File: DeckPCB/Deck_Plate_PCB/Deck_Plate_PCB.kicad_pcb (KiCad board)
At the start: 2 copper layers, 124.1 x 104 mm, 52 parts, among them J1 Raspberry_Pi_2_3, J2 NASA_Telemetry_Interface, J3 NASA PWR_Interface, J8 Board_to_Board, J9 Power, P1 Digital, P10 CONN_01X01, P11 CONN_01X01, P12 CONN_01X01, P13 CONN_01X01, P2 Power, P3 Analog, P4 Analog, P5 PWM, P6 PWM, P7 Communication, P8 CONN_01X01, P9 CONN_01X01, Q2 2N7000, Q3 2N7000, U2 LM2576T-5, U3 D24V25F9, U5 LM2576T-5, U6 SF_Logic_Level_Conv, U7 Lidar_RangeFinder, U8 ADXL377, U9 TTL_Camera

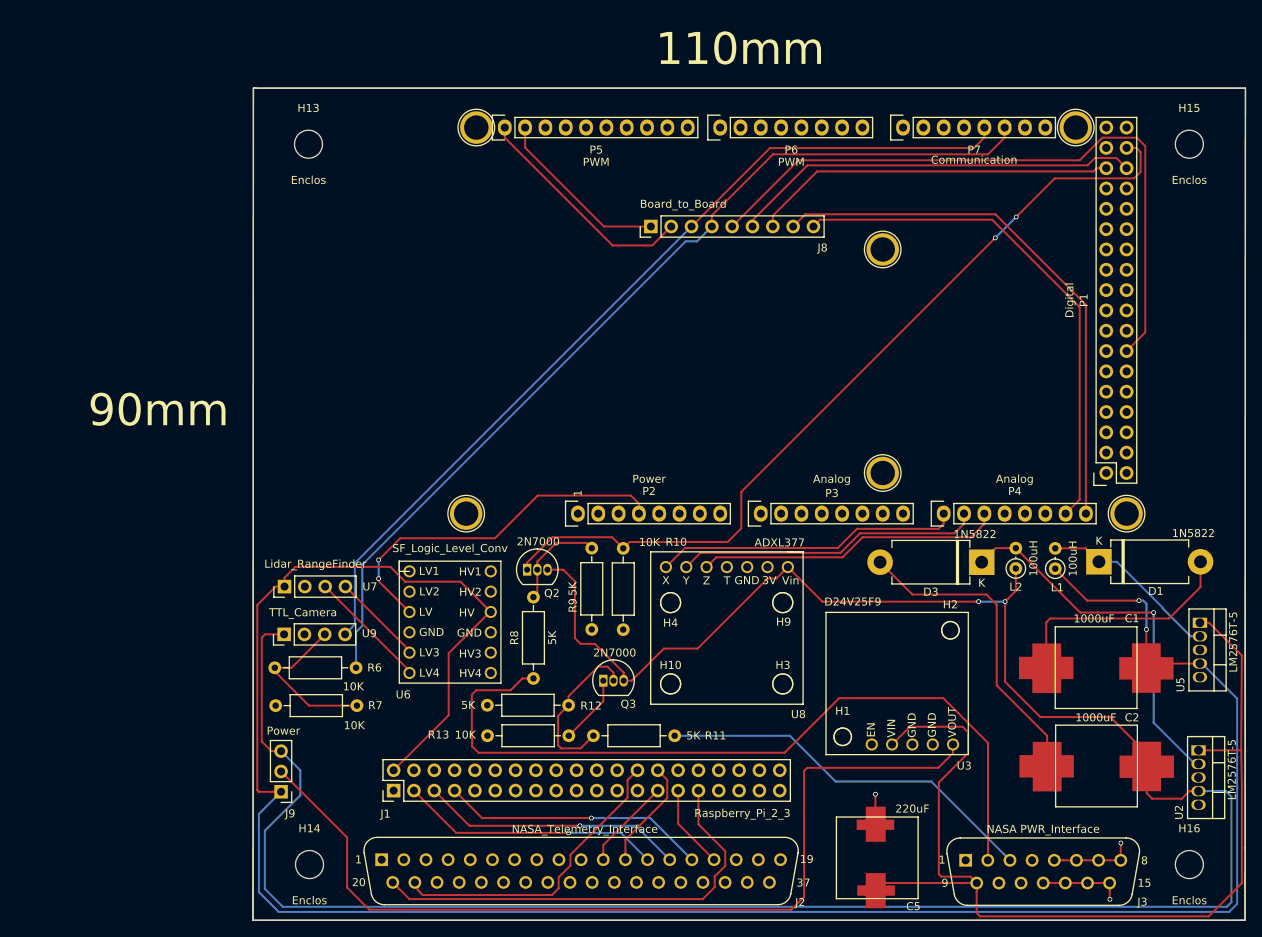
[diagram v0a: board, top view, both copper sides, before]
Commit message: Finised routing fro Main_Board, Daughter_Board, and BurnWire circuits. Creating SensorEndPanel board next.
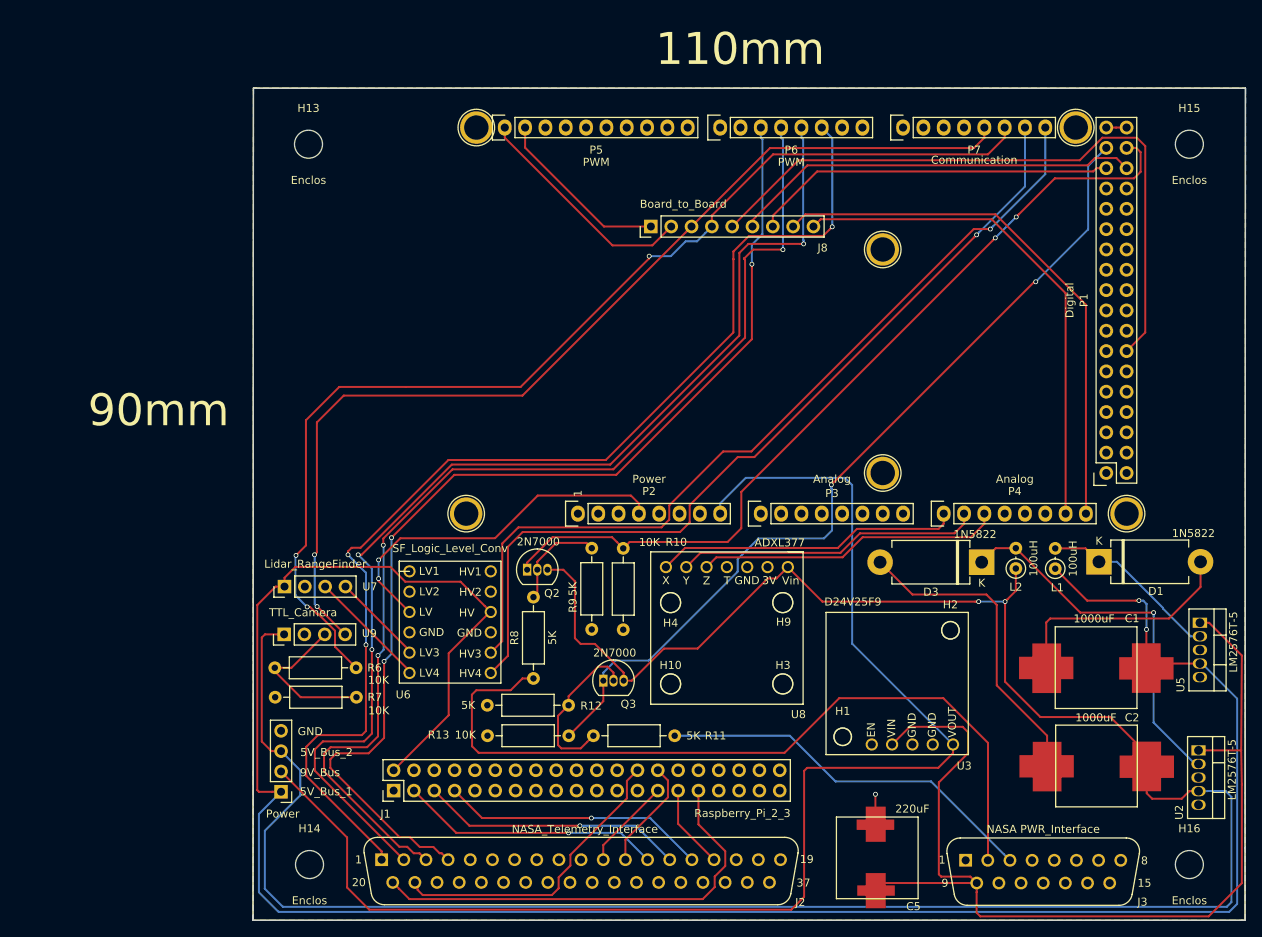
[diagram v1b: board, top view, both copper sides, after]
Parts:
- J9: footprint Connector_PinHeader_2.54mm:PinHeader_1x03_P2.54mm_Vertical -> Connector_PinHeader_2.54mm:PinHeader_1x04_P2.54mm_Vertical
- moved R7 1.05 mm to (91.8, 120.1)
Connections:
- P1 pad 35: +5V -> Net-(P1-Pad35)
- P1 pad 36: +5V -> Net-(P1-Pad35)
- P2 pad 5: +5V -> Net-(P2-Pad5)
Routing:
- net /NASA_Analog_1: track 0.00 -> 145.9 mm, vias 0 -> 3
- net /NASA_Analog_2: track 0.00 -> 141.9 mm, vias 0 -> 3
- net /NASA_Analog_3: track 0.00 -> 138.5 mm, vias 0 -> 3
- net /NASA_Analog_4: track 0.00 -> 136.2 mm, vias 0 -> 3
- net /20(SDA): track 0.00 -> 108.6 mm, vias 0 -> 1
- net /21(SCL): track 0.00 -> 108.1 mm, vias 0 -> 1
- net /TE_B: track 8.67 -> 108.7 mm, vias 0 -> 2
- net /9V_Bus: track 113.2 -> 170.4 mm
- net /TTL_RX: track 117.7 -> 139.1 mm, vias 0 -> 3
- net GND: track 24.7 -> 3.89 mm, vias 3 -> 1
- net /TTL_TX: track 111.4 -> 128.9 mm, vias 0 -> 2
- net Net-(P1-Pad35): track 0.00 -> 2.54 mm
- net /PayloadTemp: track 64.7 -> 63.3 mm
- added copper zone on B.Cu, net GND
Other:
- board text added: "5V_Bus_1"
- board text added: "5V_Bus_2"
- board text added: "9V_Bus"
- board text added: "GND"

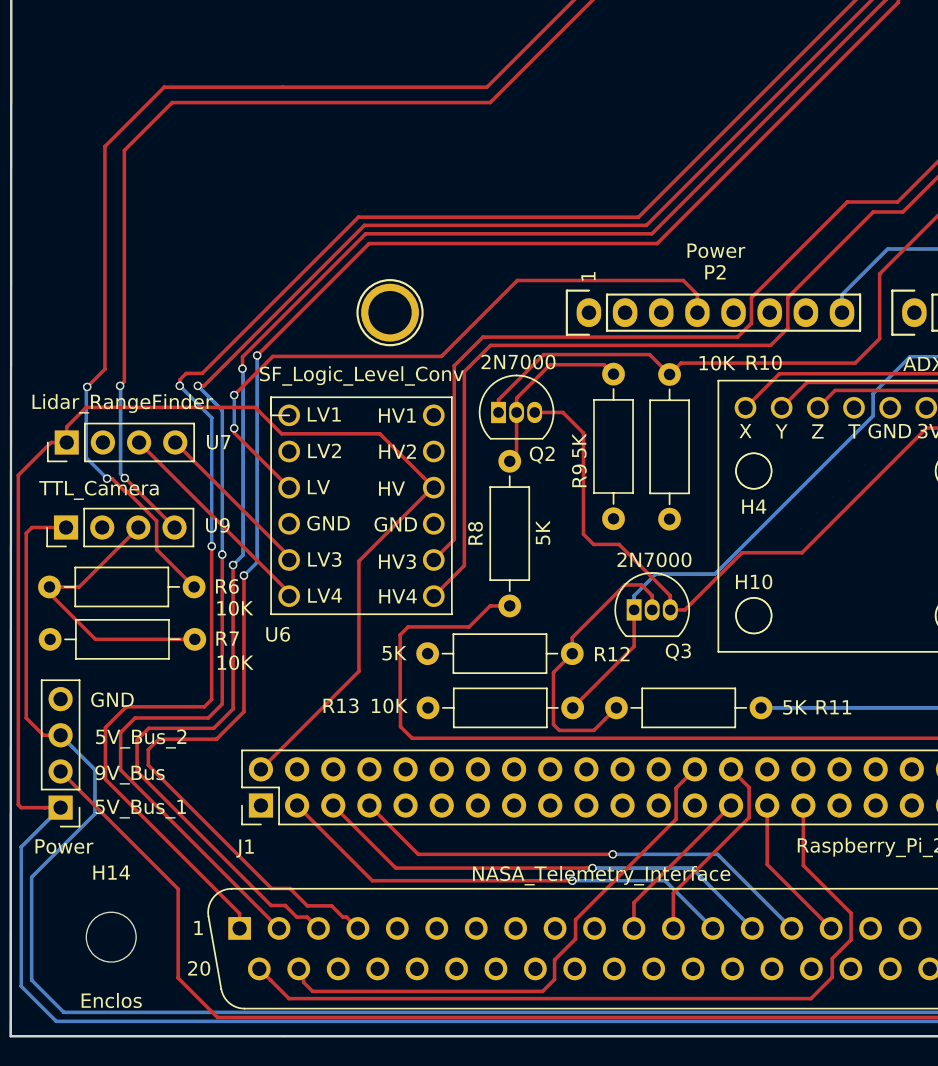
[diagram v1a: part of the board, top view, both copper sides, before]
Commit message: Added signal conditioning circuitry
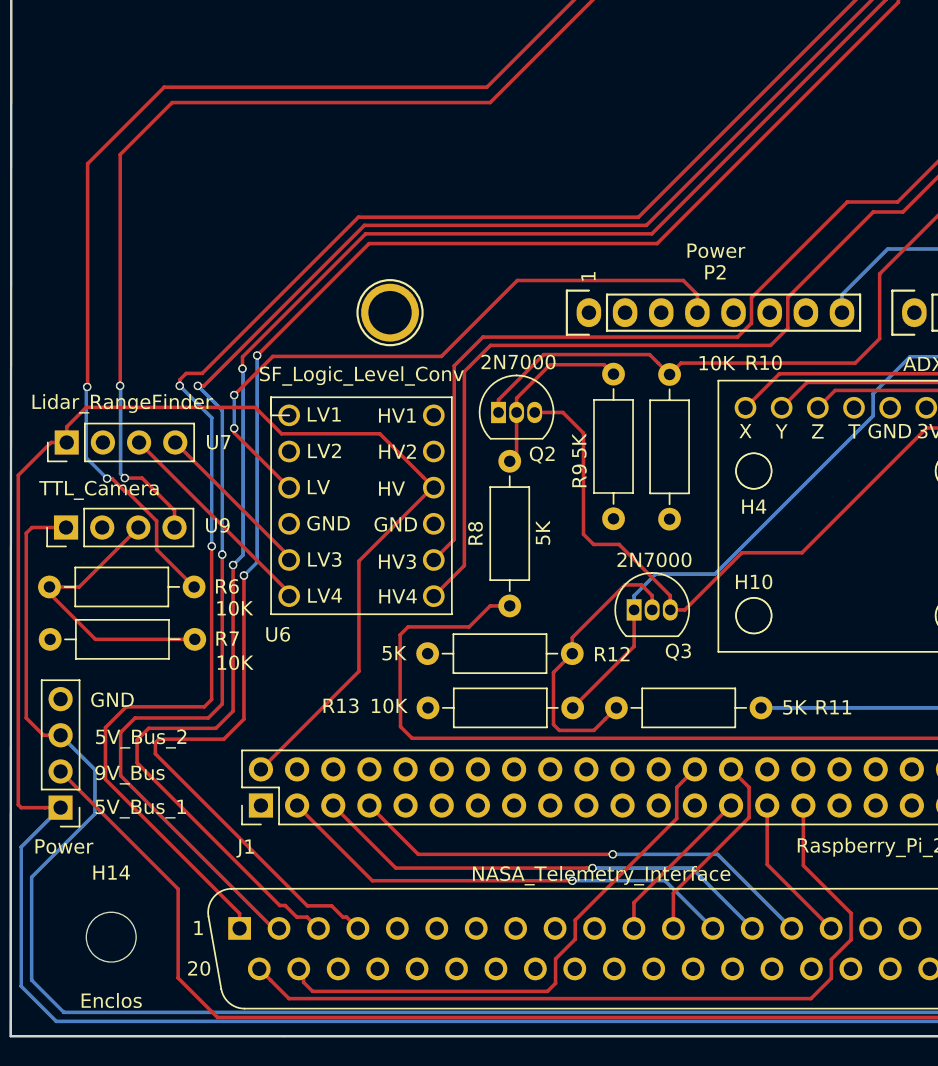
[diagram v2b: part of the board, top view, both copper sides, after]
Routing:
- net /NASA_Analog_4: track 136.2 -> 135.3 mm
- net /TTL_TX: track 128.9 -> 129.6 mm

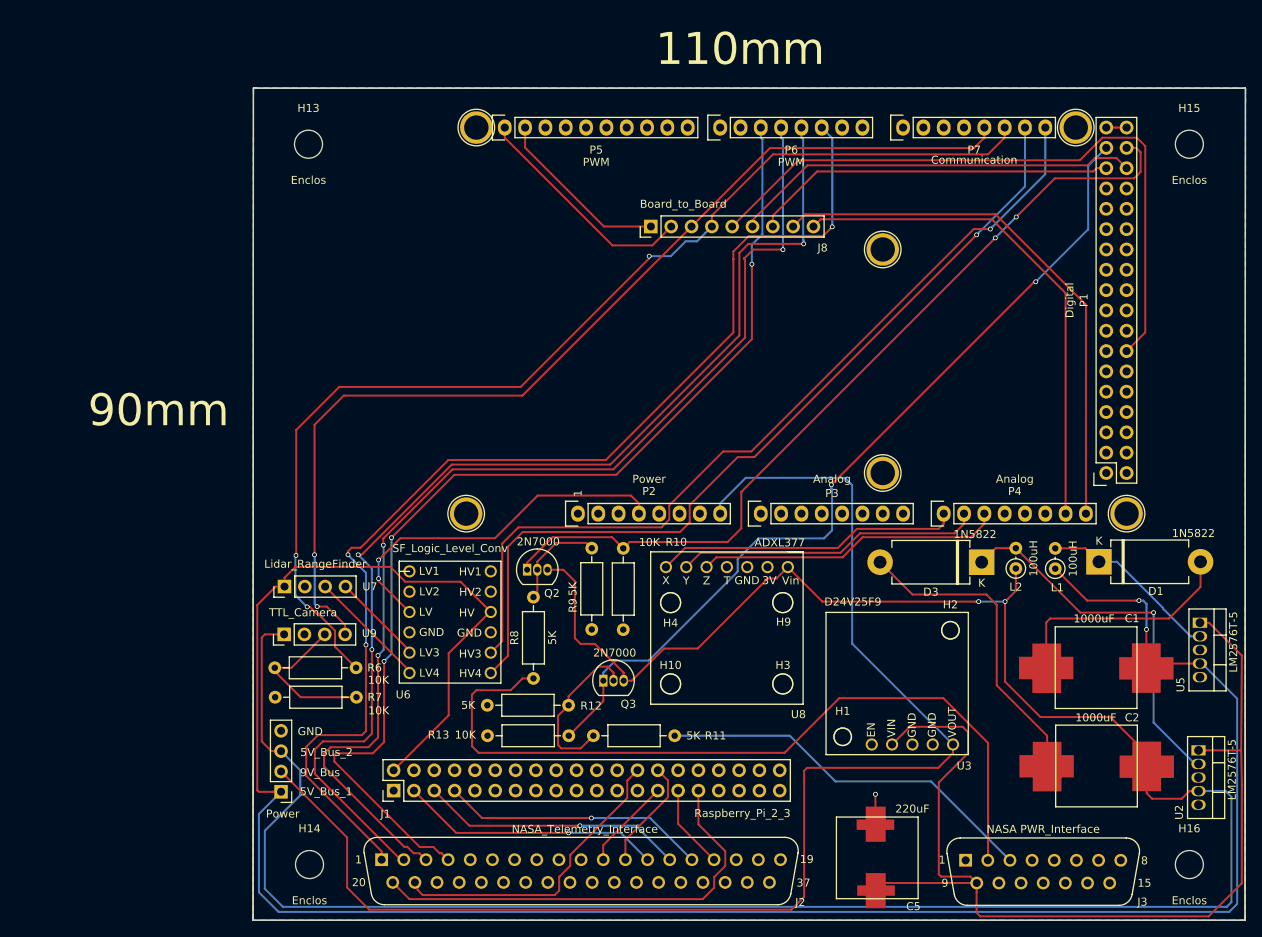
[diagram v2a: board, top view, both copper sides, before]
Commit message: Added signal conditioning circuitry and finalized main deck PCB component placement and signal tracing
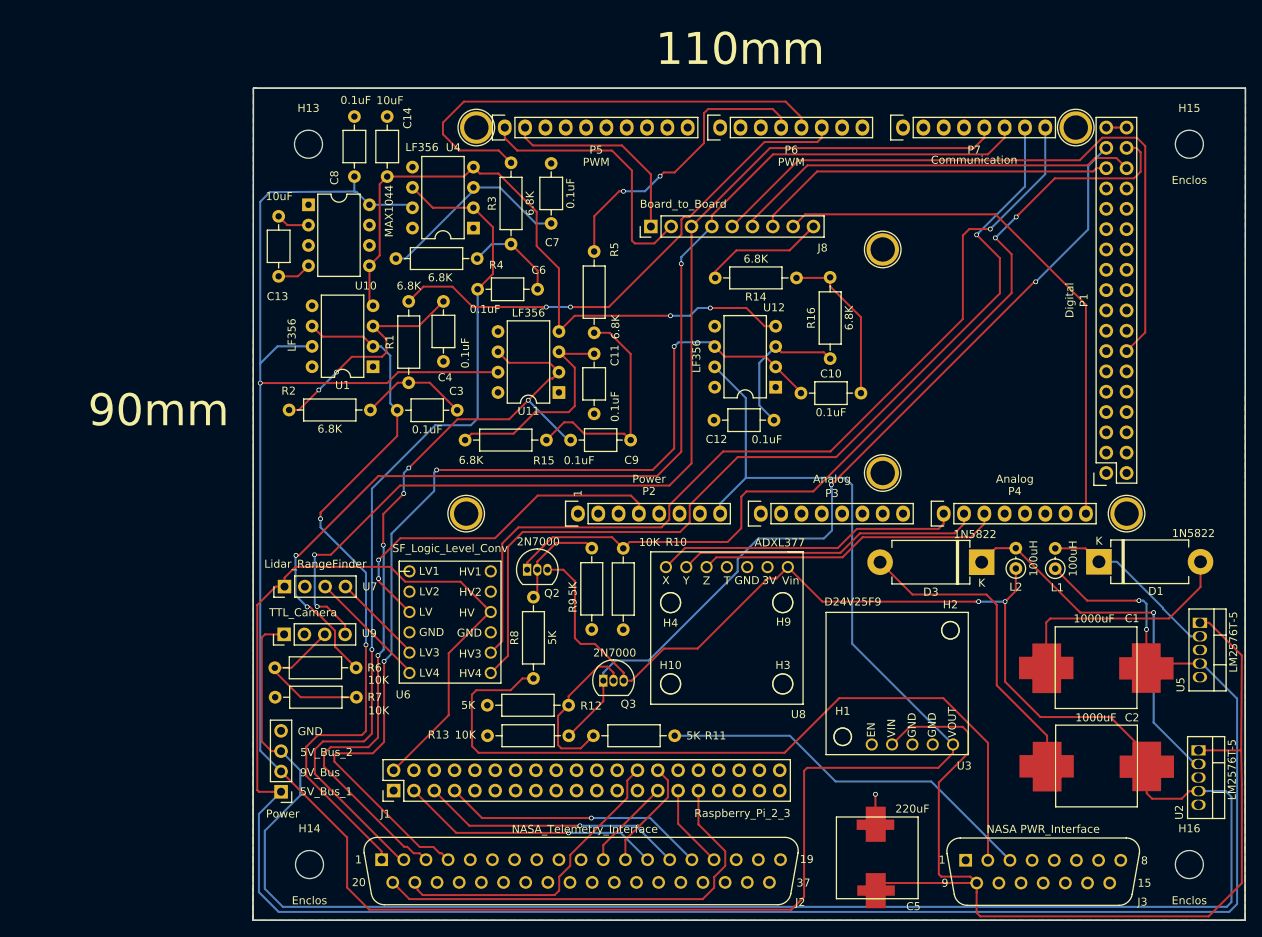
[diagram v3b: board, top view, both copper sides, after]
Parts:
- added C10: 0.1uF, Capacitor_THT:C_Axial_L3.8mm_D2.6mm_P7.50mm_Horizontal, F.Cu at (147.4, 82.1)
- added C11: 0.1uF, Capacitor_THT:C_Axial_L3.8mm_D2.6mm_P7.50mm_Horizontal, F.Cu at (121.6, 77.2)
- added C12: 0.1uF, Capacitor_THT:C_Axial_L3.8mm_D2.6mm_P7.50mm_Horizontal, F.Cu at (144.0, 85.5)
- added C13: 10uF, Capacitor_THT:C_Axial_L3.8mm_D2.6mm_P7.50mm_Horizontal, F.Cu at (82.1, 60.0)
- added C14: 10uF, Capacitor_THT:C_Axial_L3.8mm_D2.6mm_P7.50mm_Horizontal, F.Cu at (95.7, 47.5)
- added C3: 0.1uF, Capacitor_THT:C_Axial_L3.8mm_D2.6mm_P7.50mm_Horizontal, F.Cu at (96.9, 84.2)
- added C4: 0.1uF, Capacitor_THT:C_Axial_L3.8mm_D2.6mm_P7.50mm_Horizontal, F.Cu at (102.7, 70.6)
- added C6: 0.1uF, Capacitor_THT:C_Axial_L3.8mm_D2.6mm_P7.50mm_Horizontal, F.Cu at (107.0, 69.1)
- added C7: 0.1uF, Capacitor_THT:C_Axial_L3.8mm_D2.6mm_P7.50mm_Horizontal, F.Cu at (116.2, 60.9)
- added C8: 0.1uF, Capacitor_THT:C_Axial_L3.8mm_D2.6mm_P7.50mm_Horizontal, F.Cu at (91.6, 55.0)
- added C9: 0.1uF, Capacitor_THT:C_Axial_L3.8mm_D2.6mm_P7.50mm_Horizontal, F.Cu at (118.6, 88.0)
- added R1: 6.8K, Resistor_THT:R_Axial_DIN0207_L6.3mm_D2.5mm_P10.16mm_Horizontal, F.Cu at (98.4, 80.8)
- added R14: 6.8K, Resistor_THT:R_Axial_DIN0207_L6.3mm_D2.5mm_P10.16mm_Horizontal, F.Cu at (146.8, 67.7)
- added R15: 6.8K, Resistor_THT:R_Axial_DIN0207_L6.3mm_D2.5mm_P10.16mm_Horizontal, F.Cu at (105.4, 88.0)
- added R16: 6.8K, Resistor_THT:R_Axial_DIN0207_L6.3mm_D2.5mm_P10.16mm_Horizontal, F.Cu at (151.1, 77.8)
- added R2: 6.8K, Resistor_THT:R_Axial_DIN0207_L6.3mm_D2.5mm_P10.16mm_Horizontal, F.Cu at (83.4, 84.2)
- added R3: 6.8K, Resistor_THT:R_Axial_DIN0207_L6.3mm_D2.5mm_P10.16mm_Horizontal, F.Cu at (111.2, 63.5)
- added R4: 6.8K, Resistor_THT:R_Axial_DIN0207_L6.3mm_D2.5mm_P10.16mm_Horizontal, F.Cu at (96.8, 65.3)
- added R5: 6.8K, Resistor_THT:R_Axial_DIN0207_L6.3mm_D2.5mm_P10.16mm_Horizontal, F.Cu at (121.6, 74.5)
- added U1: LF356, Package_DIP:DIP-8_W7.62mm, F.Cu at (93.9, 78.8)
- added U10: MAX1044, Package_DIP:DIP-8_W7.62mm, F.Cu at (85.8, 58.5)
- added U11: LF356, Package_DIP:DIP-8_W7.62mm, F.Cu at (117.2, 82.0)
- added U12: LF356, Package_DIP:DIP-8_W7.62mm, F.Cu at (144.2, 81.3)
- added U4: LF356, Package_DIP:DIP-8_W7.62mm, F.Cu at (106.5, 61.5)
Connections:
- J2 pad 1: /NASA_Analog_1 -> /NASA_Analog_1_OUT
- J2 pad 2: /NASA_Analog_2 -> /NASA_Analog_2_OUT
- J2 pad 3: /NASA_Analog_3 -> /NASA_Analog_3_OUT
- J2 pad 4: /NASA_Analog_4 -> /NASA_Analog_4_OUT
- P4 pad 7: /PayloadTemp -> /A14
- P6 pad 3: /NASA_Analog_4 -> /5(**)
- P6 pad 4: /NASA_Analog_3 -> /NASA_Analog_3_IN
- P6 pad 5: /NASA_Analog_2 -> /NASA_Analog_2_IN
- P6 pad 6: /NASA_Analog_1 -> /NASA_Analog_1_IN
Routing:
- net /9V_Bus: track 170.4 -> 318.0 mm, vias 0 -> 1
- net /NASA_Analog_1: track 145.9 -> 0.00 mm, vias 3 -> 0
- net /NASA_Analog_2: track 142.1 -> 0.00 mm, vias 3 -> 0
- net /NASA_Analog_3: track 138.3 -> 0.00 mm, vias 3 -> 0
- net /NASA_Analog_4: track 135.3 -> 0.00 mm, vias 3 -> 0
- net /NASA_Analog_4_OUT: track 0.00 -> 126.0 mm, vias 0 -> 3
- net /NASA_Analog_2_OUT: track 0.00 -> 110.9 mm, vias 0 -> 1
- net /NASA_Analog_3_OUT: track 0.00 -> 101.8 mm, vias 0 -> 5
- net /NASA_Analog_1_OUT: track 0.00 -> 91.2 mm, vias 0 -> 2
- net /-9V_Bus: track 0.00 -> 84.1 mm, vias 0 -> 2
- net /NASA_Analog_1_IN: track 0.00 -> 64.6 mm, vias 0 -> 2
- net /NASA_Analog_2_IN: track 0.00 -> 59.4 mm
- net /PayloadTemp: track 63.3 -> 15.4 mm
- net /NASA_Analog_3_IN: track 0.00 -> 37.2 mm, vias 0 -> 2
- net Net-(C4-Pad1): track 0.00 -> 29.2 mm, vias 0 -> 2
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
